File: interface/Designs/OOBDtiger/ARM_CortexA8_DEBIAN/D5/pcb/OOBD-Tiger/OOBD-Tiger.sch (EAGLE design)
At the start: 122 parts, among them IC1 ADM3053M, IC2 ADM3053M, IC4 DS3231, U1 SY6280, U10 MP1482DS, U2 SN65HVD230(SO8), U3 SY6280, U6 SN65HVD230(SO8)

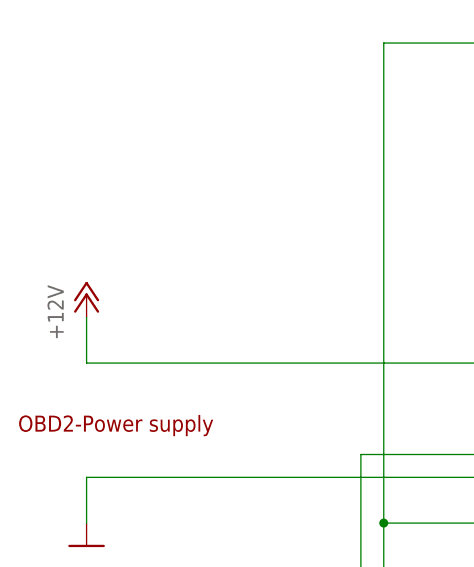
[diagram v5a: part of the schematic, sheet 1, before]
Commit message: CAN-Transceiver SN65HVD230 shift to left from adm3053
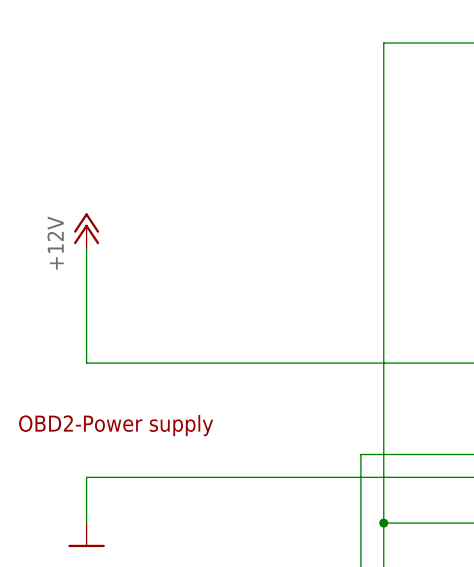
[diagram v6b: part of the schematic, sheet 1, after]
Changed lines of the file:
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@@
 <?xml version="1.0" encoding="utf-8"?>
 <!DOCTYPE eagle SYSTEM "eagle.dtd">
-<eagle version="6.4">
+<eagle version="7.6.0">
 <drawing>
 <settings>
@@
 <instance part="OOBD2-CONNECTOR" gate="A" x="66.04" y="167.64"/>
 <instance part="GND6" gate="1" x="15.24" y="162.56"/>
-<instance part="P+2" gate="1" x="15.24" y="190.5"/>
+<instance part="P+2" gate="1" x="15.24" y="198.12"/>
 <instance part="HS-CAN" gate="A" x="142.24" y="190.5" rot="R270"/>
 <instance part="IC1" gate="G$1" x="115.57" y="60.96" rot="R180"/>
@@
 <wire x1="88.9" y1="182.88" x2="15.24" y2="182.88" width="0.1524" layer="91"/>
 <pinref part="P+2" gate="1" pin="+12V"/>
-<wire x1="15.24" y1="182.88" x2="15.24" y2="187.96" width="0.1524" layer="91"/>
-</segment>
-</net>
+<wire x1="15.24" y1="182.88" x2="15.24" y2="195.58" width="0.1524" layer="91"/>
+</segment>
+</net>

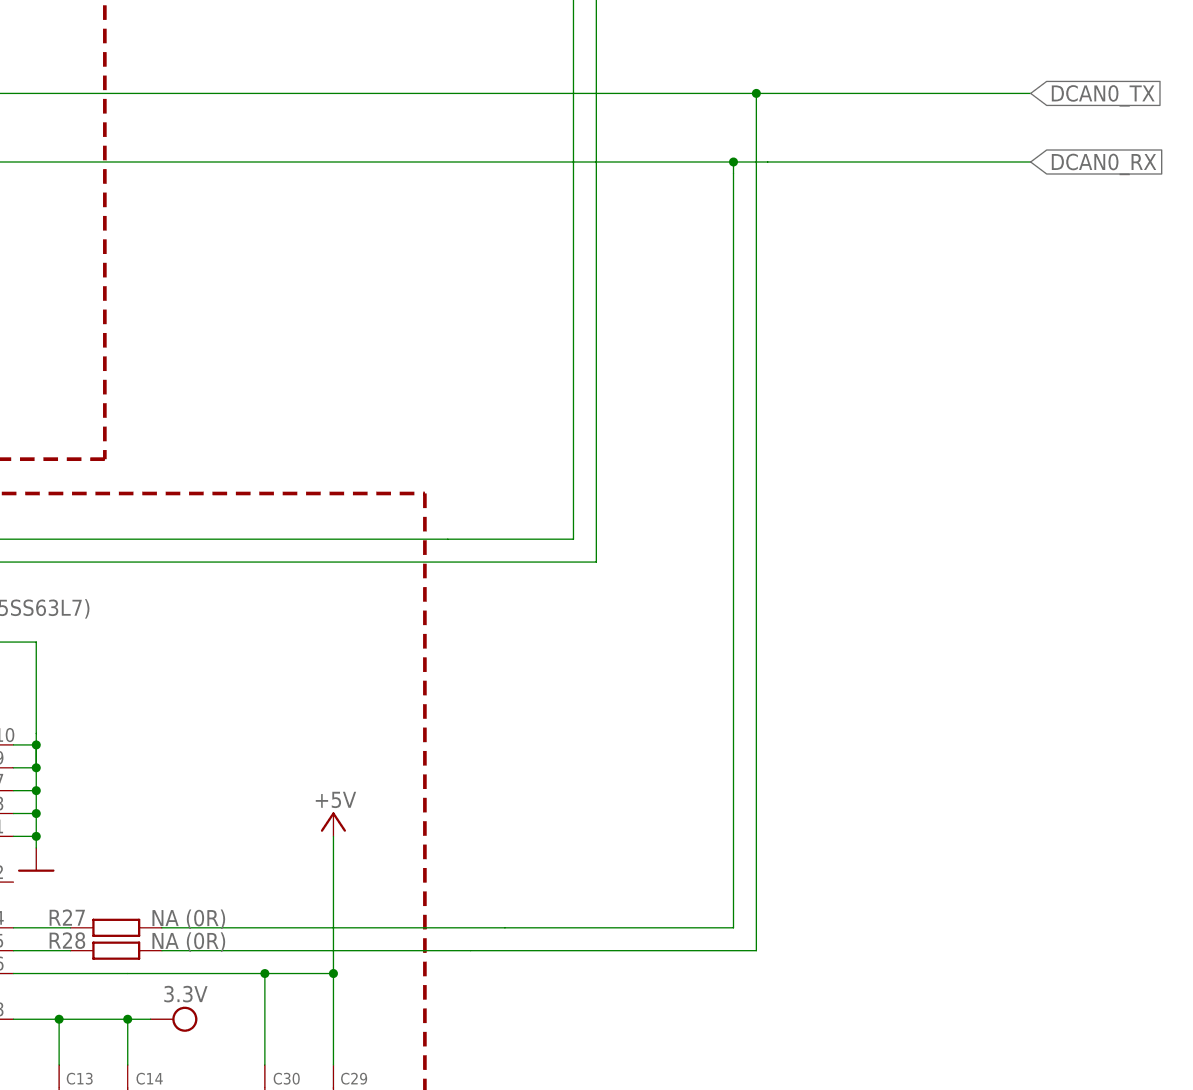
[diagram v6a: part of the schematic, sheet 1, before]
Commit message: Funktionsgruppen Powersupply & Audio endplaziert
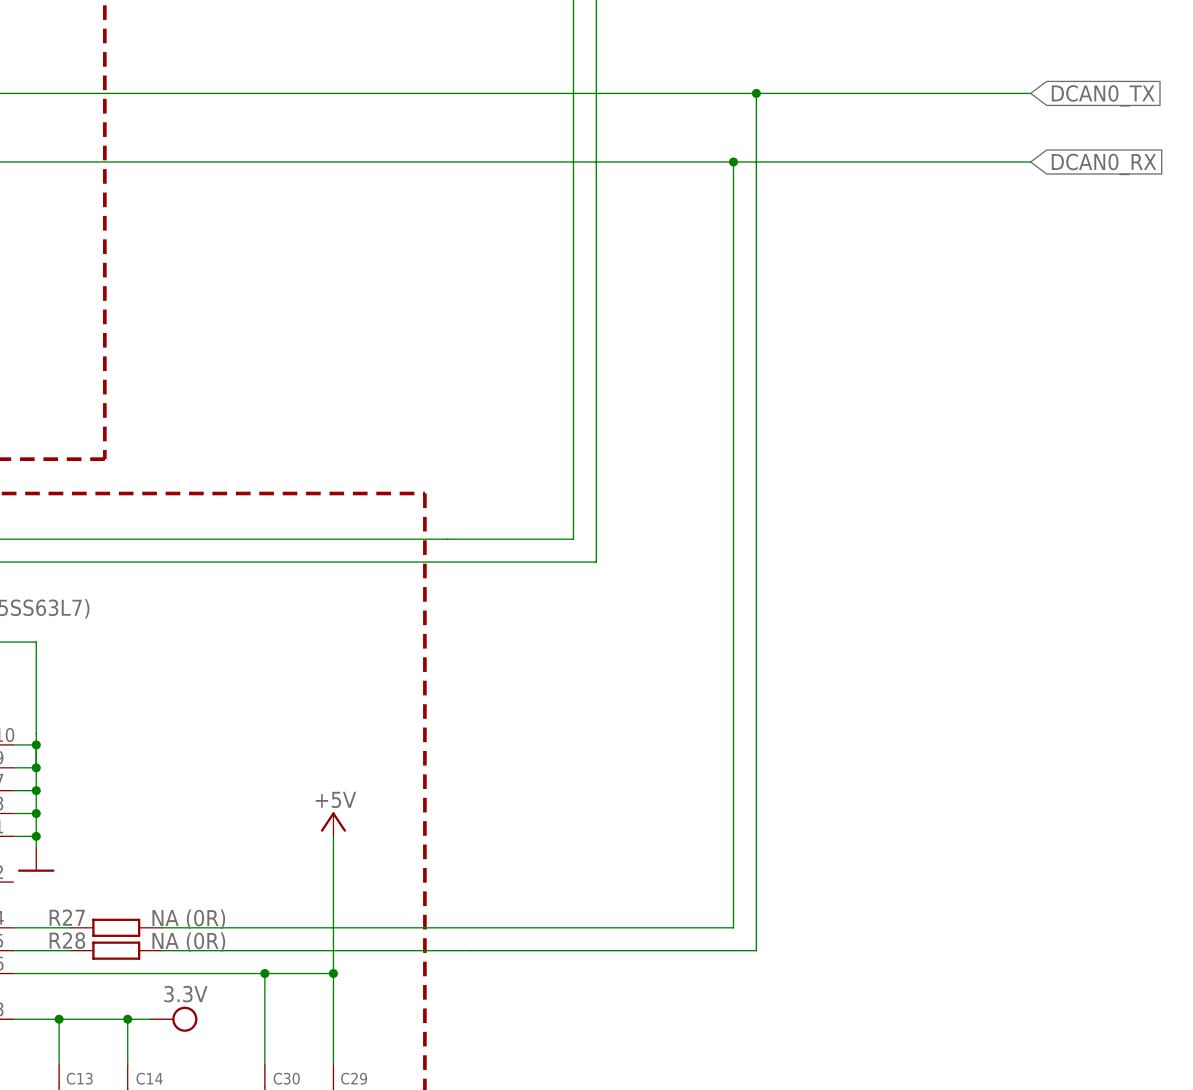
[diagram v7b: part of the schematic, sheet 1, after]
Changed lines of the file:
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@@
 <grid distance="100" unitdist="mil" unit="mil" style="lines" multiple="1" display="yes" altdistance="0.01" altunitdist="inch" altunit="inch"/>
 <layers>
-<layer number="1" name="Top" color="4" fill="1" visible="no" active="no"/>
-<layer number="2" name="Route2" color="12" fill="1" visible="no" active="no"/>
-<layer number="3" name="Route3" color="5" fill="1" visible="no" active="no"/>
-<layer number="4" name="Route4" color="1" fill="4" visible="no" active="no"/>
-<layer number="5" name="Route5" color="4" fill="4" visible="no" active="no"/>
-<layer number="6" name="Route6" color="1" fill="8" visible="no" active="no"/>
-<layer number="7" name="Route7" color="4" fill="8" visible="no" active="no"/>
-<layer number="8" name="Route8" color="1" fill="2" visible="no" active="no"/>
-<layer number="9" name="Route9" color="4" fill="2" visible="no" active="no"/>
-<layer number="10" name="Route10" color="1" fill="7" visible="no" active="no"/>
-<layer number="11" name="Route11" color="4" fill="7" visible="no" active="no"/>
-<layer number="12" name="Route12" color="1" fill="5" visible="no" active="no"/>
-<layer number="13" name="Route13" color="4" fill="5" visible="no" active="no"/>
-<layer number="14" name="Route14" color="2" fill="1" visible="no" active="no"/>
-<layer number="15" name="Route15" color="12" fill="1" visible="no" active="no"/>
-<layer number="16" name="Bottom" color="3" fill="1" visible="no" active="no"/>
-<layer number="17" name="Pads" color="2" fill="1" visible="no" active="no"/>
-<layer number="18" name="Vias" color="2" fill="1" visible="no" active="no"/>
-<layer number="19" name="Unrouted" color="6" fill="1" visible="no" active="no"/>
-<layer number="20" name="Dimension" color="7" fill="1" visible="no" active="no"/>
-<layer number="21" name="tPlace" color="7" fill="1" visible="no" active="no"/>
-<layer number="22" name="bPlace" color="6" fill="1" visible="no" active="no"/>
-<layer number="23" name="tOrigins" color="7" fill="1" visible="no" active="no"/>
-<layer number="24" name="bOrigins" color="6" fill="1" visible="no" active="no"/>
-<layer number="25" name="tNames" color="7" fill="1" visible="no" active="no"/>
-<layer number="26" name="bNames" color="6" fill="1" visible="no" active="no"/>
-<layer number="27" name="tValues" color="5" fill="1" visible="no" active="no"/>
-<layer number="28" name="bValues" color="5" fill="1" visible="no" active="no"/>
+<layer number="1" name="Top" color="4" fill="1" visible="yes" active="no"/>
+<layer number="2" name="Route2" color="12" fill="1" visible="yes" active="no"/>
+<layer number="3" name="Route3" color="5" fill="1" visible="yes" active="no"/>
+<layer number="4" name="Route4" color="1" fill="4" visible="yes" active="no"/>
+<layer number="5" name="Route5" color="4" fill="4" visible="yes" active="no"/>
+<layer number="6" name="Route6" color="1" fill="8" visible="yes" active="no"/>
+<layer number="7" name="Route7" color="4" fill="8" visible="yes" active="no"/>
+<layer number="8" name="Route8" color="1" fill="2" visible="yes" active="no"/>
+<layer number="9" name="Route9" color="4" fill="2" visible="yes" active="no"/>
+<layer number="10" name="Route10" color="1" fill="7" visible="yes" active="no"/>
+<layer number="11" name="Route11" color="4" fill="7" visible="yes" active="no"/>
+<layer number="12" name="Route12" color="1" fill="5" visible="yes" active="no"/>
+<layer number="13" name="Route13" color="4" fill="5" visible="yes" active="no"/>
+<layer number="14" name="Route14" color="2" fill="1" visible="yes" active="no"/>
+<layer number="15" name="Route15" color="12" fill="1" visible="yes" active="no"/>
+<layer number="16" name="Bottom" color="3" fill="1" visible="yes" active="no"/>
+<layer number="17" name="Pads" color="2" fill="1" visible="yes" active="no"/>
+<layer number="18" name="Vias" color="2" fill="1" visible="yes" active="no"/>
+<layer number="19" name="Unrouted" color="6" fill="1" visible="yes" active="no"/>
+<layer number="20" name="Dimension" color="7" fill="1" visible="yes" active="no"/>
+<layer number="21" name="tPlace" color="7" fill="1" visible="yes" active="no"/>
+<layer number="22" name="bPlace" color="6" fill="1" visible="yes" active="no"/>
+<layer number="23" name="tOrigins" color="7" fill="1" visible="yes" active="no"/>
+<layer number="24" name="bOrigins" color="6" fill="1" visible="yes" active="no"/>
+<layer number="25" name="tNames" color="7" fill="1" visible="yes" active="no"/>
+<layer number="26" name="bNames" color="6" fill="1" visible="yes" active="no"/>
+<layer number="27" name="tValues" color="5" fill="1" visible="yes" active="no"/>
+<layer number="28" name="bValues" color="5" fill="1" visible="yes" active="no"/>
 <layer number="29" name="tStop" color="7" fill="3" visible="no" active="no"/>
 <layer number="30" name="bStop" color="7" fill="6" visible="no" active="no"/>
@@
 <layer number="35" name="tGlue" color="7" fill="4" visible="no" active="no"/>
 <layer number="36" name="bGlue" color="7" fill="5" visible="no" active="no"/>
-<layer number="37" name="tTest" color="7" fill="1" visible="no" active="no"/>
-<layer number="38" name="bTest" color="7" fill="1" visible="no" active="no"/>
+<layer number="37" name="tTest" color="7" fill="1" visible="yes" active="no"/>
+<layer number="38" name="bTest" color="7" fill="1" visible="yes" active="no"/>
 <layer number="39" name="tKeepout" color="4" fill="11" visible="no" active="no"/>
 <layer number="40" name="bKeepout" color="3" fill="11" visible="no" active="no"/>
@@
 <layer number="44" name="Drills" color="7" fill="1" visible="no" active="no"/>
 <layer number="45" name="Holes" color="7" fill="1" visible="no" active="no"/>
-<layer number="46" name="Milling" color="3" fill="1" visible="no" active="no"/>
-<layer number="47" name="Measures" color="7" fill="1" visible="no" active="no"/>
-<layer number="48" name="Document" color="5" fill="1" visible="no" active="no"/>
-<layer number="49" name="Reference" color="7" fill="1" visible="no" active="no"/>
-<layer number="50" name="dxf" color="7" fill="1" visible="no" active="no"/>
-<layer number="51" name="tDocu" color="7" fill="1" visible="no" active="no"/>
-<layer number="52" name="bDocu" color="7" fill="1" visible="no" active="no"/>
-<layer number="53" name="tGND_GNDA" color="7" fill="9" visible="no" active="no"/>
-<layer number="54" name="bGND_GNDA" color="1" fill="9" visible="no" active="no"/>
-<layer number="56" name="wert" color="7" fill="1" visible="no" active="no"/>
-<layer number="57" name="tCAD" color="7" fill="1" visible="no" active="no"/>
-<layer number="59" name="tCarbon" color="7" fill="1" visible="no" active="no"/>
-<layer number="60" name="bCarbon" color="7" fill="1" visible="no" active="no"/>
+<layer number="46" name="Milling" color="3" fill="1" visible="yes" active="no"/>
+<layer number="47" name="Measures" color="7" fill="1" visible="yes" active="no"/>
+<layer number="48" name="Document" color="5" fill="1" visible="yes" active="no"/>
+<layer number="49" name="Reference" color="7" fill="1" visible="yes" active="no"/>
+<layer number="50" name="dxf" color="7" fill="1" visible="yes" active="no"/>
+<layer number="51" name="tDocu" color="7" fill="1" visible="yes" active="no"/>
+<layer number="52" name="bDocu" color="7" fill="1" visible="yes" active="no"/>
+<layer number="53" name="tGND_GNDA" color="7" fill="9" visible="yes" active="no"/>
+<layer number="54" name="bGND_GNDA" color="1" fill="9" visible="yes" active="no"/>
+<layer number="56" name="wert" color="7" fill="1" visible="yes" active="no"/>
+<layer number="57" name="tCAD" color="7" fill="1" visible="yes" active="no"/>
+<layer number="59" name="tCarbon" color="7" fill="1" visible="yes" active="no"/>
+<layer number="60" name="bCarbon" color="7" fill="1" visible="yes" active="no"/>
 <layer number="90" name="Modules" color="5" fill="1" visible="no" active="yes"/>
 <layer number="91" name="Nets" color="2" fill="1" visible="yes" active="yes"/>
@@
 <net name="DCAN0_RX" class="0">
 <segment>
-<wire x1="351.79" y1="139.7" x2="322.58" y2="139.7" width="0.1524" layer="91"/>
+<wire x1="351.79" y1="139.7" x2="318.77" y2="139.7" width="0.1524" layer="91"/>
 <pinref part="U6" gate="G$1" pin="RXD"/>
 <label x="351.79" y="139.7" size="1.778" layer="95" xref="yes"/>
 <pinref part="R27" gate="G$1" pin="2"/>
-<wire x1="322.58" y1="139.7" x2="318.77" y2="139.7" width="0.1524" layer="91"/>
 <wire x1="318.77" y1="139.7" x2="193.04" y2="139.7" width="0.1524" layer="91"/>
-<wire x1="255.27" y1="54.61" x2="293.37" y2="54.61" width="0.1524" layer="91"/>
-<wire x1="293.37" y1="54.61" x2="318.77" y2="54.61" width="0.1524" layer="91"/>
-<wire x1="318.77" y1="54.61" x2="318.77" y2="138.43" width="0.1524" layer="91"/>
-<wire x1="318.77" y1="138.43" x2="318.77" y2="139.7" width="0.1524" layer="91"/>
+<wire x1="255.27" y1="54.61" x2="318.77" y2="54.61" width="0.1524" layer="91"/>
+<wire x1="318.77" y1="54.61" x2="318.77" y2="139.7" width="0.1524" layer="91"/>
 <junction x="318.77" y="139.7"/>
 </segment>
